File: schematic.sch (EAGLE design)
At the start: 22 parts, among them U1 ADP3338AKCZ-3.3RL7

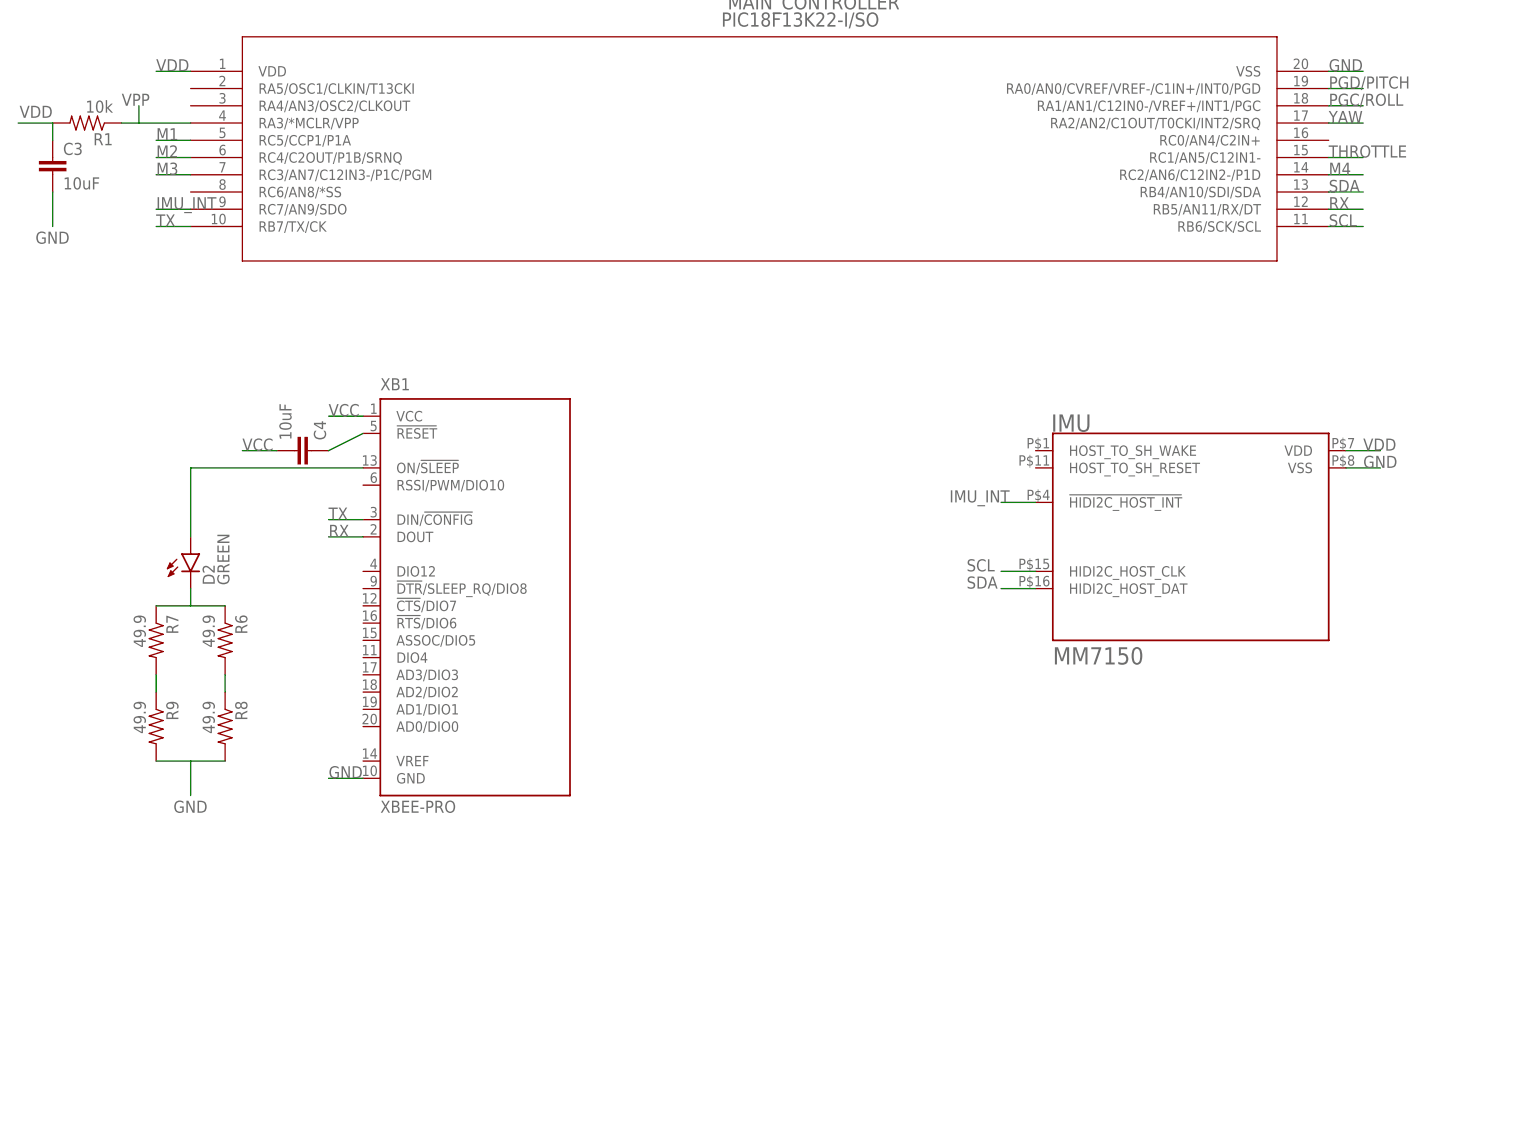
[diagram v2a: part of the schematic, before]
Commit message: Added missing connections for IMU and XBEE. Added inturrupt pin for XBEE.
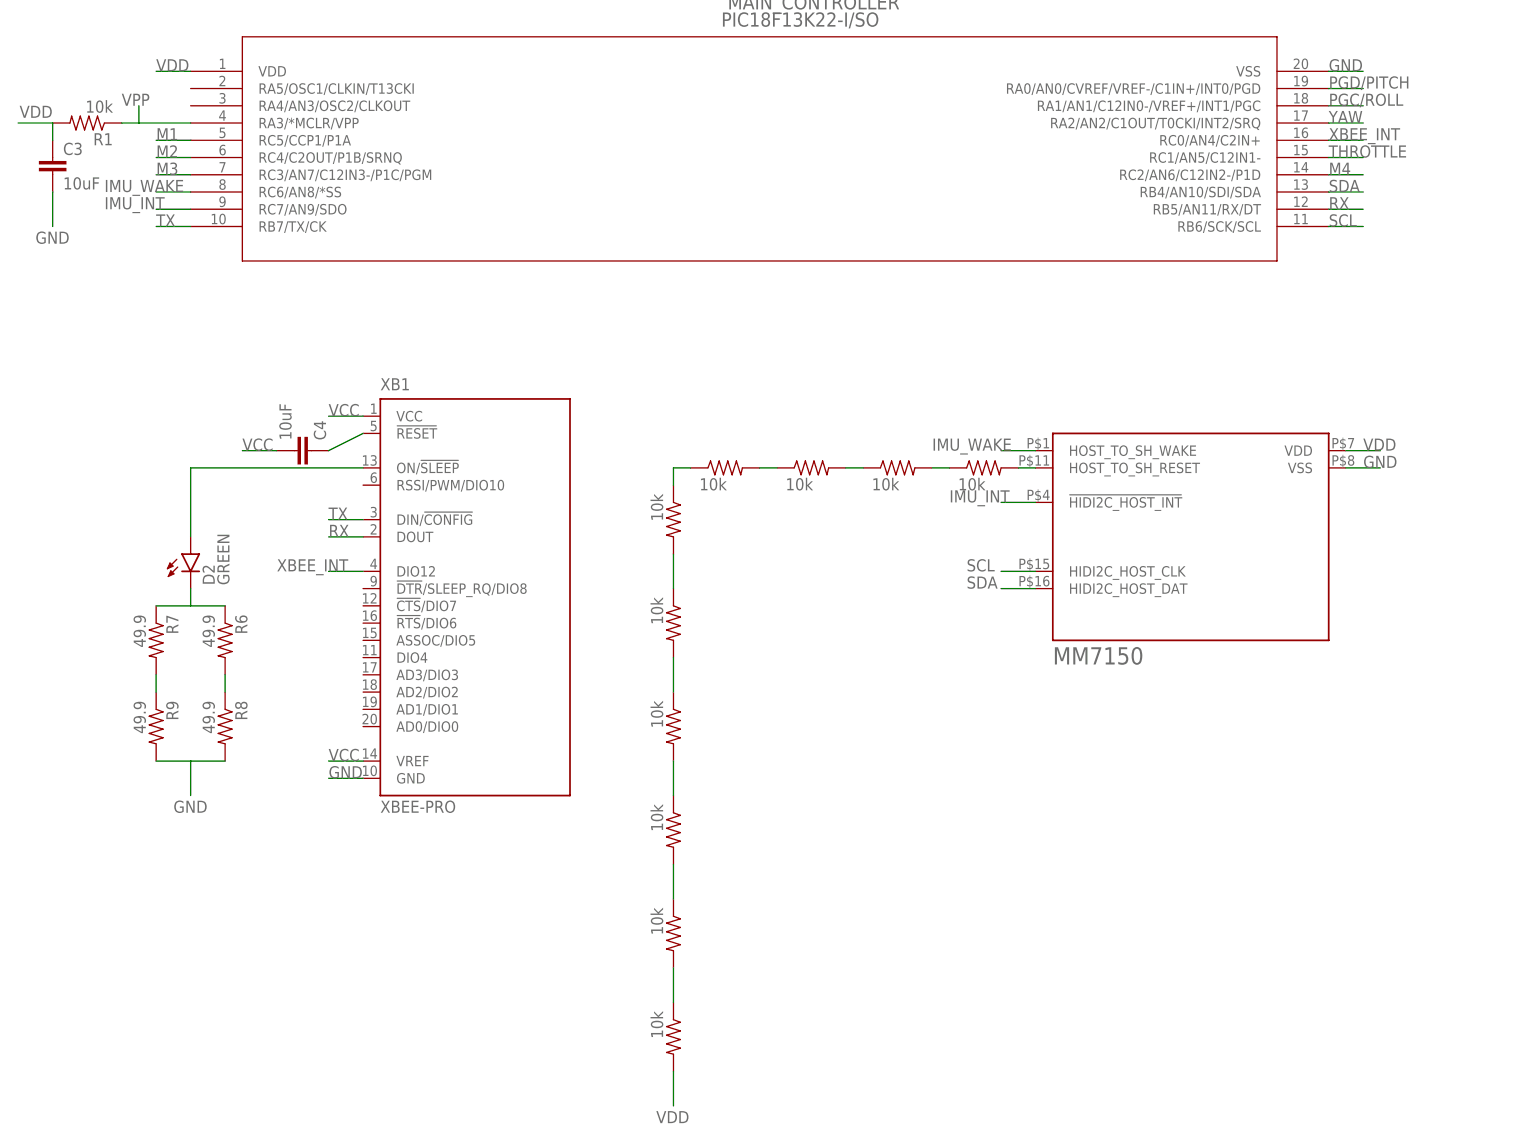
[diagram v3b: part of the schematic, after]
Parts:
- added R10, R11, R12, R13, R14, R15, R16, R17, R18, R19: 10k, SparkFun-Passives:RESISTOR0402-RES
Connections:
- new net IMU_WAKE: IMU.HOST_TO_SH_WAKE, MAIN_CONTROLLER.RC6/AN8/*SS
- new net N$10: IMU.HOST_TO_SH_RESET, R10.2
- new net N$11: R10.1, R11.2
- new net N$12: R11.1, R12.2
- new net N$13: R12.1, R13.2
- new net N$14: R13.1, R14.1
- new net N$15: R14.2, R15.1
- new net N$16: R15.2, R16.1
- new net N$17: R16.2, R17.1
- new net N$18: R17.2, R18.1
- new net N$19: R18.2, R19.1
- new net XBEE_INT: MAIN_CONTROLLER.RC0/AN4/C2IN+, XB1.DIO12
- net VCC: now also XB1.VREF
- net VDD: now also R19.2
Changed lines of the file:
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@@
 <part name="R8" library="SparkFun-Passives" deviceset="RESISTOR" device="0402-RES" value="49.9"/>
 <part name="R9" library="SparkFun-Passives" deviceset="RESISTOR" device="0402-RES" value="49.9"/>
+<part name="R10" library="SparkFun-Passives" deviceset="RESISTOR" device="0402-RES" value="10k"/>
+<part name="R11" library="SparkFun-Passives" deviceset="RESISTOR" device="0402-RES" value="10k"/>
+<part name="R12" library="SparkFun-Passives" deviceset="RESISTOR" device="0402-RES" value="10k"/>
+<part name="R13" library="SparkFun-Passives" deviceset="RESISTOR" device="0402-RES" value="10k"/>
+<part name="R14" library="SparkFun-Passives" deviceset="RESISTOR" device="0402-RES" value="10k"/>
+<part name="R15" library="SparkFun-Passives" deviceset="RESISTOR" device="0402-RES" value="10k"/>
+<part name="R16" library="SparkFun-Passives" deviceset="RESISTOR" device="0402-RES" value="10k"/>
+<part name="R17" library="SparkFun-Passives" deviceset="RESISTOR" device="0402-RES" value="10k"/>
+<part name="R18" library="SparkFun-Passives" deviceset="RESISTOR" device="0402-RES" value="10k"/>
+<part name="R19" library="SparkFun-Passives" deviceset="RESISTOR" device="0402-RES" value="10k"/>
 </parts>
 <sheets>
@@
 <instance part="C2" gate="G$1" x="190.5" y="50.8"/>
 <instance part="C3" gate="G$1" x="-20.32" y="-15.24"/>
-<instance part="IMU" gate="A" x="147.32" y="-68.58"/>
+<instance part="IMU" gate="A" x="147.32" y="-68.58" smashed="yes">
+<attribute name="VALUE" x="127" y="-87.376" size="2.54" layer="96"/>
+</instance>
 <instance part="XB1" gate="G$1" x="40.64" y="-76.2"/>
 <instance part="C4" gate="G$1" x="15.24" y="-55.88" rot="MR90"/>
@@
 <instance part="R8" gate="G$1" x="5.08" y="-96.52" rot="R270"/>
 <instance part="R9" gate="G$1" x="-5.08" y="-96.52" rot="R270"/>
+<instance part="R10" gate="G$1" x="116.84" y="-58.42" smashed="yes">
+<attribute name="VALUE" x="113.03" y="-61.722" size="1.778" layer="96"/>
+</instance>
+<instance part="R11" gate="G$1" x="104.14" y="-58.42" smashed="yes">
+<attribute name="VALUE" x="100.33" y="-61.722" size="1.778" layer="96"/>
+</instance>
+<instance part="R12" gate="G$1" x="91.44" y="-58.42" smashed="yes">
+<attribute name="VALUE" x="87.63" y="-61.722" size="1.778" layer="96"/>
+</instance>
+<instance part="R13" gate="G$1" x="78.74" y="-58.42" smashed="yes">
+<attribute name="VALUE" x="74.93" y="-61.722" size="1.778" layer="96"/>
+</instance>
+<instance part="R14" gate="G$1" x="71.12" y="-66.04" smashed="yes" rot="R270">
+<attribute name="VALUE" x="67.818" y="-62.23" size="1.778" layer="96" rot="R270"/>
+</instance>
+<instance part="R15" gate="G$1" x="71.12" y="-81.28" smashed="yes" rot="R270">
+<attribute name="VALUE" x="67.818" y="-77.47" size="1.778" layer="96" rot="R270"/>
+</instance>
+<instance part="R16" gate="G$1" x="71.12" y="-96.52" smashed="yes" rot="R270">
+<attribute name="VALUE" x="67.818" y="-92.71" size="1.778" layer="96" rot="R270"/>
+</instance>
+<instance part="R17" gate="G$1" x="71.12" y="-111.76" smashed="yes" rot="R270">
+<attribute name="VALUE" x="67.818" y="-107.95" size="1.778" layer="96" rot="R270"/>
+</instance>
+<instance part="R18" gate="G$1" x="71.12" y="-127" smashed="yes" rot="R270">
+<attribute name="VALUE" x="67.818" y="-123.19" size="1.778" layer="96" rot="R270"/>
+</instance>
+<instance part="R19" gate="G$1" x="71.12" y="-142.24" smashed="yes" rot="R270">
+<attribute name="VALUE" x="67.818" y="-138.43" size="1.778" layer="96" rot="R270"/>
+</instance>
 </instances>
 <busses>
@@
 <label x="172.72" y="-55.88" size="1.778" layer="95"/>
 </segment>
+<segment>
+<pinref part="R19" gate="G$1" pin="2"/>
+<wire x1="71.12" y1="-147.32" x2="71.12" y2="-152.4" width="0.1524" layer="91"/>
+<label x="68.58" y="-154.94" size="1.778" layer="95"/>
+</segment>
 </net>
 <net name="VSS" class="0">
@@
 <label x="7.62" y="-55.88" size="1.778" layer="95"/>
 </segment>
+<segment>
+<pinref part="XB1" gate="G$1" pin="VREF"/>
+<wire x1="25.4" y1="-101.6" x2="20.32" y2="-101.6" width="0.1524" layer="91"/>
+<label x="20.32" y="-101.6" size="1.778" layer="95"/>
+</segment>
 </net>
 <net name="SCL" class="0">
@@
 <pinref part="MAIN_CONTROLLER" gate="A" pin="RC7/AN9/SDO"/>
 <wire x1="0" y1="-20.32" x2="-5.08" y2="-20.32" width="0.1524" layer="91"/>
-<label x="-5.08" y="-20.32" size="1.778" layer="95"/>
+<label x="-12.7" y="-20.32" size="1.778" layer="95"/>
 </segment>
 </net>
@@
 </segment>
 </net>
+<net name="N$10" class="0">
+<segment>
+<pinref part="IMU" gate="A" pin="HOST_TO_SH_RESET"/>
+<pinref part="R10" gate="G$1" pin="2"/>
+<wire x1="124.46" y1="-58.42" x2="121.92" y2="-58.42" width="0.1524" layer="91"/>
+</segment>
+</net>
+<net name="N$11" class="0">
+<segment>
+<pinref part="R10" gate="G$1" pin="1"/>
+<pinref part="R11" gate="G$1" pin="2"/>
+<wire x1="111.76" y1="-58.42" x2="109.22" y2="-58.42" width="0.1524" layer="91"/>
+</segment>
+</net>
+<net name="N$12" class="0">
+<segment>
+<pinref part="R11" gate="G$1" pin="1"/>
+<pinref part="R12" gate="G$1" pin="2"/>
+<wire x1="99.06" y1="-58.42" x2="96.52" y2="-58.42" width="0.1524" layer="91"/>
+</segment>
+</net>
+<net name="N$13" class="0">
+<segment>
+<pinref part="R12" gate="G$1" pin="1"/>
+<pinref part="R13" gate="G$1" pin="2"/>
+<wire x1="86.36" y1="-58.42" x2="83.82" y2="-58.42" width="0.1524" layer="91"/>
+</segment>
+</net>
+<net name="N$14" class="0">
+<segment>
+<pinref part="R13" gate="G$1" pin="1"/>
+<pinref part="R14" gate="G$1" pin="1"/>
+<wire x1="73.66" y1="-58.42" x2="71.12" y2="-58.42" width="0.1524" layer="91"/>
+<wire x1="71.12" y1="-58.42" x2="71.12" y2="-60.96" width="0.1524" layer="91"/>
+</segment>
+</net>
+<net name="N$15" class="0">
+<segment>
+<pinref part="R14" gate="G$1" pin="2"/>
+<pinref part="R15" gate="G$1" pin="1"/>
+<wire x1="71.12" y1="-71.12" x2="71.12" y2="-76.2" width="0.1524" layer="91"/>
+</segment>
+</net>
+<net name="N$16" class="0">
+<segment>
+<pinref part="R15" gate="G$1" pin="2"/>
+<pinref part="R16" gate="G$1" pin="1"/>
+<wire x1="71.12" y1="-86.36" x2="71.12" y2="-91.44" width="0.1524" layer="91"/>
+</segment>
+</net>
+<net name="N$17" class="0">
+<segment>
+<pinref part="R16" gate="G$1" pin="2"/>
+<pinref part="R17" gate="G$1" pin="1"/>
+<wire x1="71.12" y1="-101.6" x2="71.12" y2="-106.68" width="0.1524" layer="91"/>
+</segment>
+</net>
+<net name="N$18" class="0">
+<segment>
+<pinref part="R17" gate="G$1" pin="2"/>
+<pinref part="R18" gate="G$1" pin="1"/>
+<wire x1="71.12" y1="-116.84" x2="71.12" y2="-121.92" width="0.1524" layer="91"/>
+</segment>
+</net>
+<net name="N$19" class="0">
+<segment>
+<pinref part="R18" gate="G$1" pin="2"/>
+<pinref part="R19" gate="G$1" pin="1"/>
+<wire x1="71.12" y1="-132.08" x2="71.12" y2="-137.16" width="0.1524" layer="91"/>
+</segment>
+</net>
+<net name="IMU_WAKE" class="0">
+<segment>
+<pinref part="MAIN_CONTROLLER" gate="A" pin="RC6/AN8/*SS"/>
+<wire x1="0" y1="-17.78" x2="-5.08" y2="-17.78" width="0.1524" layer="91"/>
+<label x="-12.7" y="-17.78" size="1.778" layer="95"/>
+</segment>
+<segment>
+<pinref part="IMU" gate="A" pin="HOST_TO_SH_WAKE"/>
+<wire x1="124.46" y1="-55.88" x2="119.38" y2="-55.88" width="0.1524" layer="91"/>
+<label x="109.22" y="-55.88" size="1.778" layer="95"/>
+</segment>
+</net>
+<net name="XBEE_INT" class="0">
+<segment>
+<pinref part="MAIN_CONTROLLER" gate="A" pin="RC0/AN4/C2IN+"/>
+<wire x1="167.64" y1="-10.16" x2="172.72" y2="-10.16" width="0.1524" layer="91"/>
+<label x="167.64" y="-10.16" size="1.778" layer="95"/>
+</segment>
+<segment>
+<pinref part="XB1" gate="G$1" pin="DIO12"/>
+<wire x1="25.4" y1="-73.66" x2="20.32" y2="-73.66" width="0.1524" layer="91"/>
+<label x="12.7" y="-73.66" size="1.778" layer="95"/>
+</segment>
+</net>

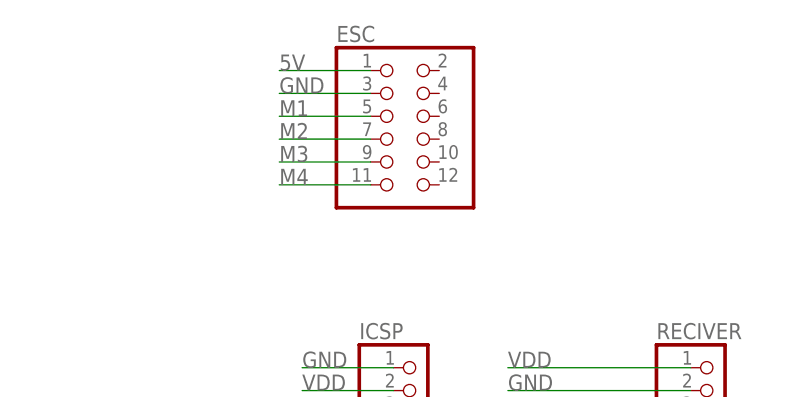
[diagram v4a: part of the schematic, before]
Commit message: Repositioned components to reduce number of jumber cables needed
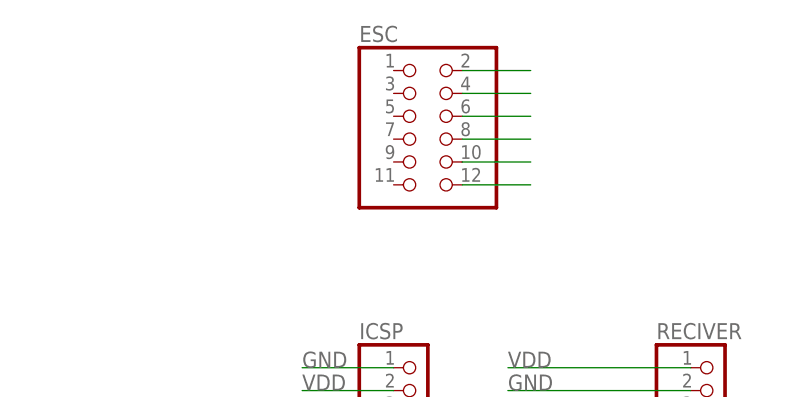
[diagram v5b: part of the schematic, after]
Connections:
- net 5V: now also ESC.2; no longer ESC.1
- net GND: now also ESC.4; no longer ESC.3
- net M1: now also ESC.6; no longer ESC.5
- net M2: now also ESC.8; no longer ESC.7
- net M3: now also ESC.10; no longer ESC.9
- net M4: now also ESC.12; no longer ESC.11
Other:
- moved on the sheet: ESC
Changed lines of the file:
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@@
 <instance part="U1" gate="A" x="170.18" y="48.26"/>
 <instance part="ICSP" gate="A" x="99.06" y="45.72"/>
-<instance part="ESC" gate="A" x="96.52" y="81.28"/>
+<instance part="ESC" gate="A" x="99.06" y="81.28"/>
 <instance part="RECIVER" gate="A" x="132.08" y="45.72"/>
 <instance part="C1" gate="G$1" x="149.86" y="50.8"/>
@@
 </segment>
 <segment>
-<pinref part="ESC" gate="A" pin="1"/>
-<wire x1="93.98" y1="86.36" x2="83.82" y2="86.36" width="0.1524" layer="91"/>
-<label x="83.82" y="86.36" size="1.778" layer="95"/>
+<pinref part="ESC" gate="A" pin="2"/>
+<wire x1="104.14" y1="86.36" x2="111.76" y2="86.36" width="0.1524" layer="91"/>
 </segment>
 </net>
@@
 <wire x1="152.4" y1="43.18" x2="144.78" y2="43.18" width="0.1524" layer="91"/>
 <label x="144.78" y="43.18" size="1.778" layer="95"/>
-</segment>
-<segment>
-<pinref part="ESC" gate="A" pin="3"/>
-<wire x1="93.98" y1="83.82" x2="83.82" y2="83.82" width="0.1524" layer="91"/>
-<label x="83.82" y="83.82" size="1.778" layer="95"/>
 </segment>
 <segment>
@@
 <label x="-2.54" y="-109.22" size="1.778" layer="95"/>
 </segment>
+<segment>
+<pinref part="ESC" gate="A" pin="4"/>
+<wire x1="104.14" y1="83.82" x2="111.76" y2="83.82" width="0.1524" layer="91"/>
+</segment>
 </net>
 <net name="M1" class="0">
-<segment>
-<pinref part="ESC" gate="A" pin="5"/>
-<wire x1="93.98" y1="81.28" x2="83.82" y2="81.28" width="0.1524" layer="91"/>
-<label x="83.82" y="81.28" size="1.778" layer="95"/>
-</segment>
 <segment>
 <pinref part="MAIN_CONTROLLER" gate="A" pin="RC5/CCP1/P1A"/>
@@
 <label x="-5.08" y="-10.16" size="1.778" layer="95"/>
 </segment>
+<segment>
+<pinref part="ESC" gate="A" pin="6"/>
+<wire x1="104.14" y1="81.28" x2="111.76" y2="81.28" width="0.1524" layer="91"/>
+</segment>
 </net>
 <net name="M2" class="0">
-<segment>
-<pinref part="ESC" gate="A" pin="7"/>
-<wire x1="93.98" y1="78.74" x2="83.82" y2="78.74" width="0.1524" layer="91"/>
-<label x="83.82" y="78.74" size="1.778" layer="95"/>
-</segment>
 <segment>
 <pinref part="MAIN_CONTROLLER" gate="A" pin="RC4/C2OUT/P1B/SRNQ"/>
@@
 <label x="-5.08" y="-12.7" size="1.778" layer="95"/>
 </segment>
+<segment>
+<pinref part="ESC" gate="A" pin="8"/>
+<wire x1="104.14" y1="78.74" x2="111.76" y2="78.74" width="0.1524" layer="91"/>
+</segment>
 </net>
 <net name="M3" class="0">
-<segment>
-<pinref part="ESC" gate="A" pin="9"/>
-<wire x1="93.98" y1="76.2" x2="83.82" y2="76.2" width="0.1524" layer="91"/>
-<label x="83.82" y="76.2" size="1.778" layer="95"/>
-</segment>
 <segment>
 <pinref part="MAIN_CONTROLLER" gate="A" pin="RC3/AN7/C12IN3-/P1C/PGM"/>
@@
 <label x="-5.08" y="-15.24" size="1.778" layer="95"/>
 </segment>
+<segment>
+<pinref part="ESC" gate="A" pin="10"/>
+<wire x1="104.14" y1="76.2" x2="111.76" y2="76.2" width="0.1524" layer="91"/>
+</segment>
 </net>
 <net name="M4" class="0">
-<segment>
-<pinref part="ESC" gate="A" pin="11"/>
-<wire x1="93.98" y1="73.66" x2="83.82" y2="73.66" width="0.1524" layer="91"/>
-<label x="83.82" y="73.66" size="1.778" layer="95"/>
-</segment>
 <segment>
 <pinref part="MAIN_CONTROLLER" gate="A" pin="RC2/AN6/C12IN2-/P1D"/>
@@
 <label x="167.64" y="-15.24" size="1.778" layer="95"/>
 </segment>
-</net>
+<segment>
+<pinref part="ESC" gate="A" pin="12"/>
+<wire x1="104.14" y1="73.66" x2="111.76" y2="73.66" width="0.1524" layer="91"/>
+</segment>
+</net>
